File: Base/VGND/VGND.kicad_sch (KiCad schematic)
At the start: 40 parts, among them J1 Conn_01x04_Pin, J2 Conn_01x05_Pin, J3 Barrel_Jack_Switch, J4 AudioJack2_Ground, J5 AudioJack2_Ground, Q1 40V, U1 TLE2426xD, U2 OPA1656

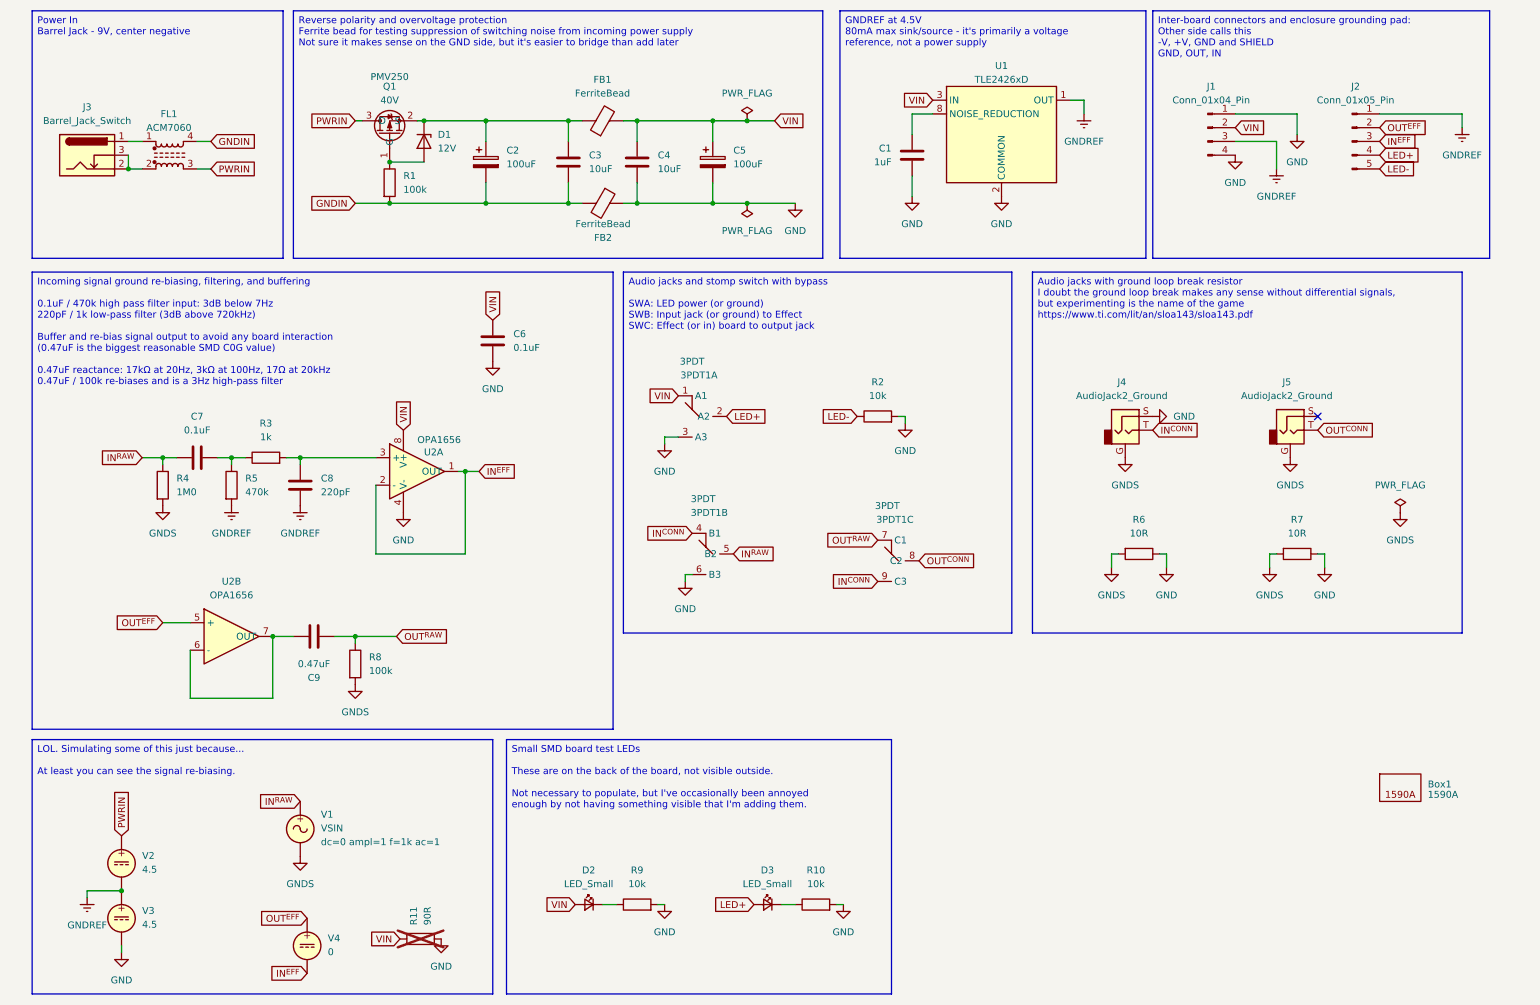
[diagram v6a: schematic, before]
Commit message: VGND: Add capacitor to GNDREF for stability
The base boards should use GNDREF purely as a voltage reference, but
let's face it, they haven't always done that.  Hopefully no longer
calling it GND will keep it from happening, but this adds a small
capacitor to it in the hope that it will help keep it stable.

The TLE2426 datasheet has a graph of the stability range on pg 17 on
load current vs load capacitance, and that says that it should be stable
with a load capacitance in the 1uF-100uF range for all valid output
currents (+-20mA).

So adding a 10uF capacitor on the base board should be the safe thing to
do.  There's nothing we can do if the effect board just pulls or sinks
more current than the 20mA that the TLE2426 supports, but we can at
least stay off the documented unstable region.

[ From a quick look through the effect boards, it looks like we should
  be good. GNDREF is typically used with the inverting input of an
  op-amp. Or alternatively with sufficiently big resistors to the
  signal, ie tens of kOhms or more. Fingers crossed. ]

Also fix the incorrect commentary about 80mA current capability on the
schematic sheet.  I wonder where I picked that incorrect value from.  I
must have been looking at the wrong part.  Or on some bad meds.

Signed-off-by: Linus Torvalds <torvalds@linux-foundation.org>
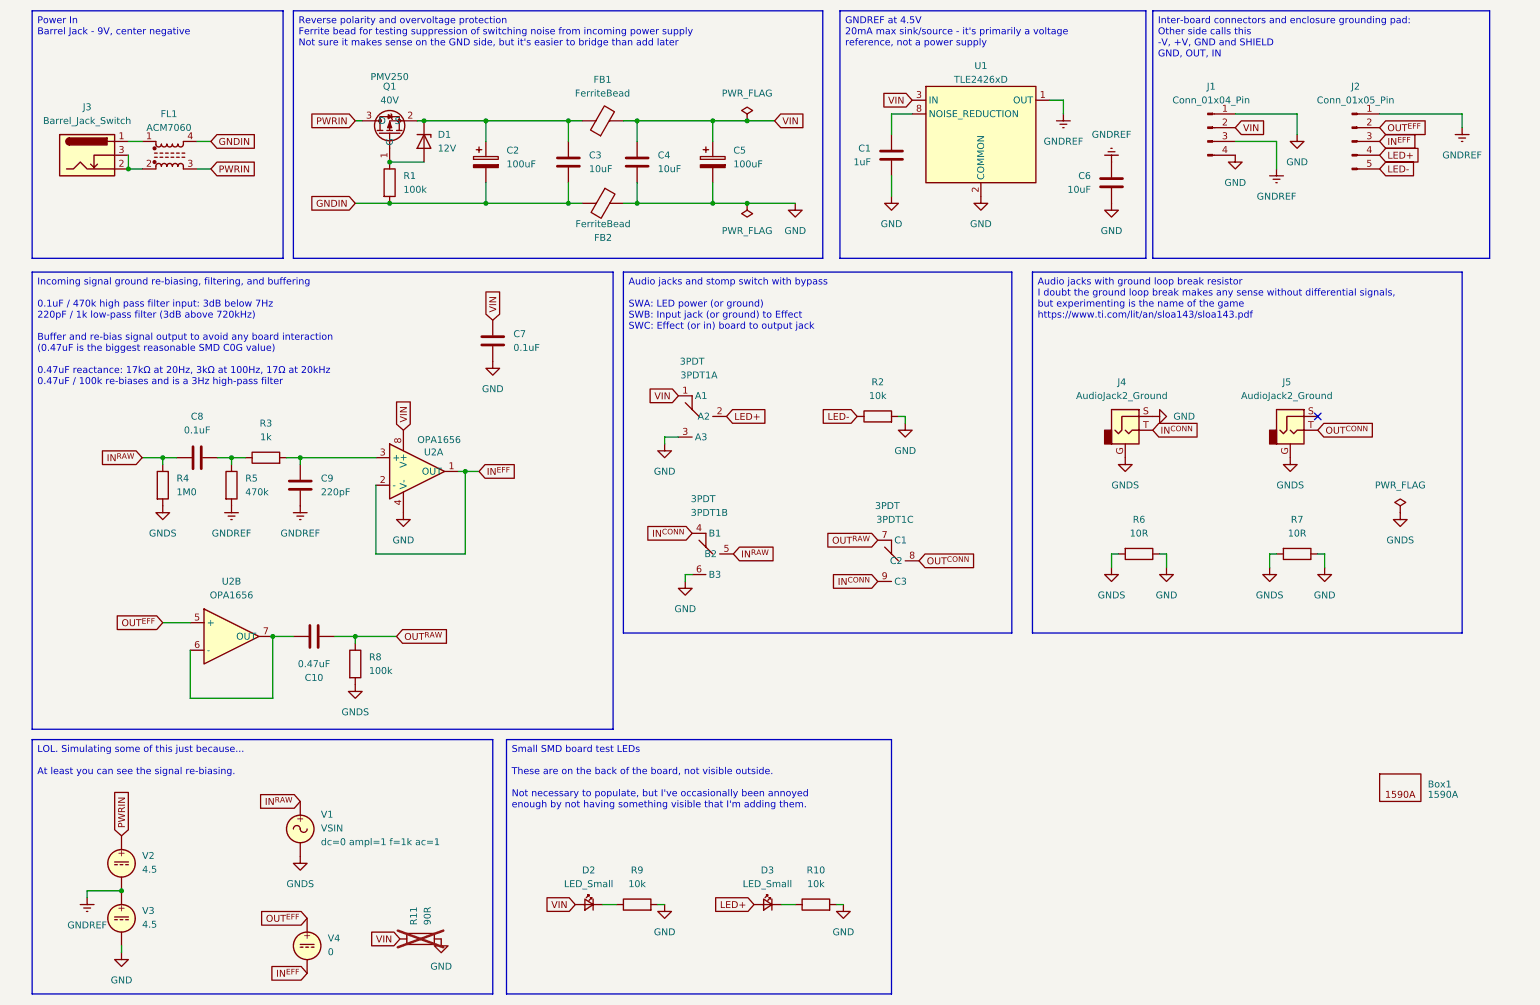
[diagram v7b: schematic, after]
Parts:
- added C6: 10uF, Capacitor_SMD:C_1206_3216Metric_Pad1.33x1.80mm_HandSolder, symbol Device:C
- renumbered C9 to C10, C6 to C7, C7 to C8, C8 to C9
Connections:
- net GND: now also C6.2
- net GNDREF: now also C6.1
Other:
- moved on the sheet: C1, U1

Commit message: VGND: use the Würth reverse-mounted LEDs
Let's make those pointless status lights that you can't see in an
enclosure really fancy.

Because let's face it, most of my testing is without enclosures.

Signed-off-by: Linus Torvalds <torvalds@linux-foundation.org>
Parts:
- D2, D3: footprint LED_SMD:LED_0805_2012Metric_Pad1.15x1.40mm_HandSolder -> Mylib:Würth Reverse Mount LED
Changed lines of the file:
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@@
 			)
 		)
-		(property "Footprint" "LED_SMD:LED_0805_2012Metric_Pad1.15x1.40mm_HandSolder"
+		(property "Footprint" "Mylib:Würth Reverse Mount LED"
 			(at 116.84 179.07 90)
 			(effects
@@
 			)
 		)
-		(property "Footprint" "LED_SMD:LED_0805_2012Metric_Pad1.15x1.40mm_HandSolder"
+		(property "Footprint" "Mylib:Würth Reverse Mount LED"
 			(at 149.86 179.07 90)
 			(effects
